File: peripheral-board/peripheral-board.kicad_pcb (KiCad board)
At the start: 2 copper layers, 165 x 100 mm, 152 parts, among them CON1001 AVR-ISP-10, IC1001 ATTINY48-A, P1001 Peripheral Bus, P1002 Power, P9001 VGA, P9002 VGA DSUB, SW2001 1, SW2002 2, SW2003 3, SW2004 4, SW2005 5, SW2006 6, SW2007 7, SW2008 8, SW2009 9, SW2010 0, SW2011 +, SW2012 ´, SW2013 BKSP, SW2014 TROLL, SW2015 §, SW2016 UP, SW2017 RMB, SW2018 Q, SW2019 W, SW2020 E, SW2021 R, SW2022 T, SW2023 Y, SW2024 U, SW2025 I, SW2026 O, SW2027 P, SW2028 Å, SW2029 ¨, SW2030 RETURN, SW2031 ALT_GR, SW2032 <, SW2033 LEFT, SW2034 MMB, SW2035 A, SW2036 S, SW2037 D, SW2038 F, SW2039 G, SW2040 H, SW2041 J, SW2042 K, SW2043 L, SW2044 Ö, SW2045 Ä, SW2046 ', SW2047 ESC, SW2048 TAB, SW2049 ALT, SW2050 DOWN, SW2051 LMB, SW2052 SHIFT_L, SW2053 Z, SW2054 X, SW2055 C, SW2056 V, SW2057 B, SW2058 N, SW2059 M, SW2060 ,, SW2061 ., SW2062 -, SW2063 SHIFT_R, SW2064 FN_R, SW2065 SPACE, SW2066 FN_L, SW2067 RIGHT, SW2068 CTRL, SW2069 SPACE, U2001 4017, U2002 4017, U2003 74HC00, U6001 TCA0372

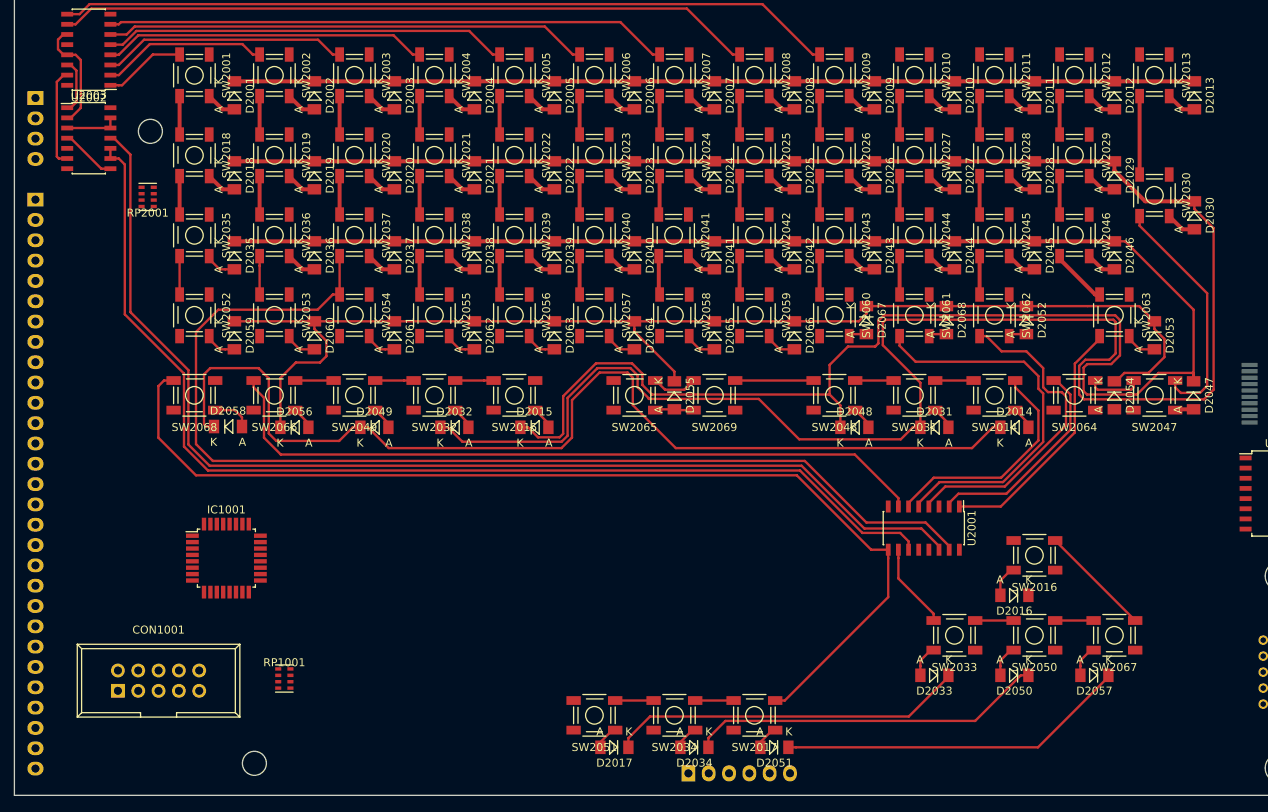
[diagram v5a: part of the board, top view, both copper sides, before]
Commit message: some more keyboard stuff fit on this side..
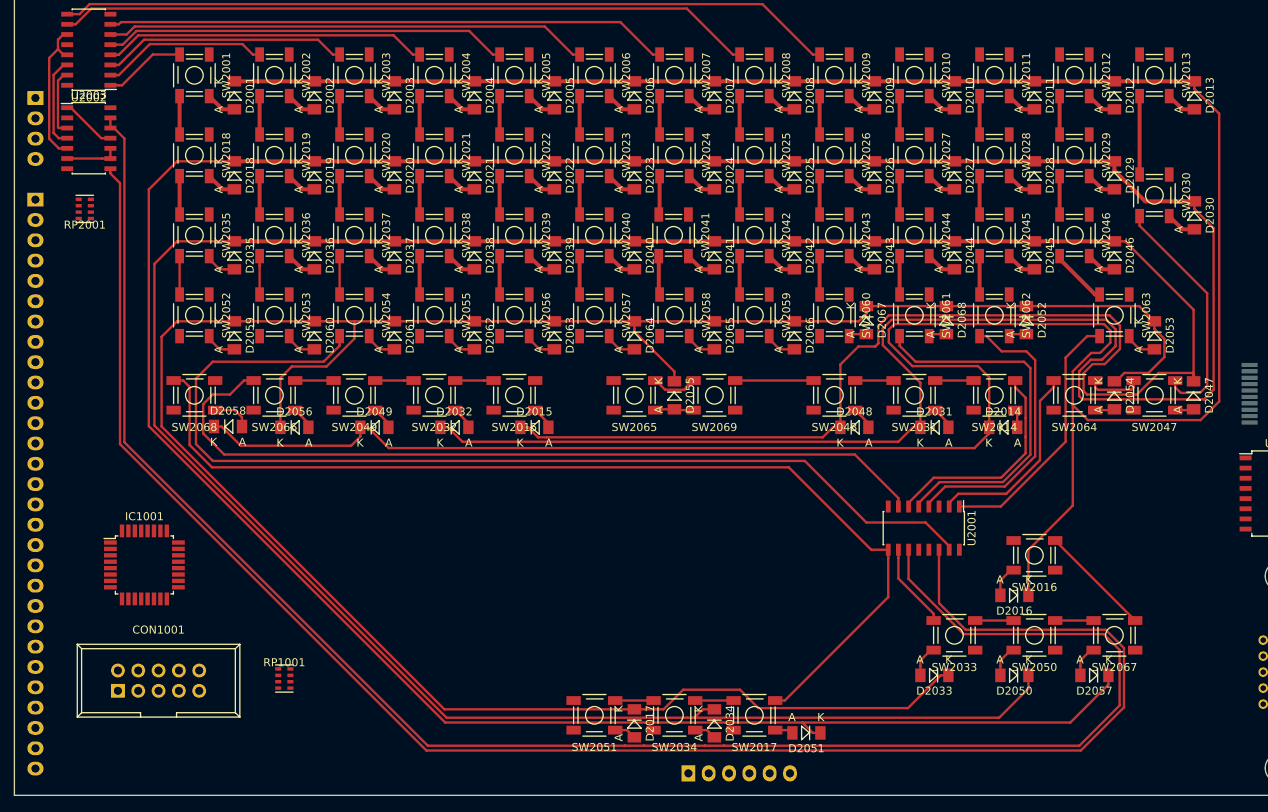
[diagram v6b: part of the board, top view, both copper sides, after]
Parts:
- removed REF** (x2): 3mm, Mounting_Holes:MountingHole_3mm
- moved IC1001 10.3 mm to (101.2, 121.2)
- moved RP2001 8.00 mm to (93.8, 76.7)
- moved D2051 4.39 mm to (184.0, 142.2)
- moved D2017 3.91 mm to (162.5, 141.0), turned to 270 degrees
- moved D2034 3.91 mm to (172.5, 141.0), turned to 270 degrees
- moved D2014 1.40 mm to (208.6, 104.0)
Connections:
- D2017 pad 1: /Keyboard/Q1 -> /Keyboard/Q3
- D2033 pad 1: /Keyboard/Q1 -> /Keyboard/Q3
- D2051 pad 1: /Keyboard/Q3 -> /Keyboard/Q1
- D2057 pad 1: /Keyboard/Q3 -> /Keyboard/Q1
- U2003 pad 1: /Keyboard/CLK -> Net-(U2003-Pad1)
- U2003 pad 10: Net-(U2001-Pad11) -> Net-(U2003-Pad10)
- U2003 pad 11: Net-(U2001-Pad14) -> Net-(U2003-Pad1)
- U2003 pad 12: Net-(U2003-Pad12) -> Net-(U2001-Pad11)
- U2003 pad 13: Net-(U2003-Pad12) -> Net-(U2001-Pad11)
- U2003 pad 2: Net-(U2002-Pad11) -> /Keyboard/~RESET
- U2003 pad 3: Net-(U2003-Pad12) -> Net-(U2002-Pad15)
- U2003 pad 4: Net-(U2003-Pad4) -> /Keyboard/CLK
- U2003 pad 5: /Keyboard/~RESET -> Net-(U2002-Pad11)
- U2003 pad 6: Net-(U2002-Pad15) -> Net-(U2003-Pad10)
- U2003 pad 8: Net-(U2003-Pad4) -> Net-(U2001-Pad14)
- U2003 pad 9: Net-(U2001-Pad11) -> Net-(U2003-Pad10)
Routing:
- net /Keyboard/Q1: track 339.0 -> 464.8 mm
- net /Keyboard/Q0: track 250.7 -> 372.0 mm
- net /Keyboard/Q2: track 302.9 -> 409.6 mm
- net /Keyboard/Q3: track 201.1 -> 297.0 mm
- net Net-(U2001-Pad11): track 138.2 -> 225.3 mm
- net Net-(U2001-Pad14): track 142.1 -> 219.0 mm
- net /Keyboard/COL14: track 105.6 -> 116.9 mm
- net Net-(U2003-Pad12): track 7.57 -> 0.00 mm
- net Net-(U2003-Pad4): track 7.43 -> 0.00 mm
- net Net-(U2003-Pad1): track 0.00 -> 7.43 mm
- net Net-(U2003-Pad10): track 0.00 -> 7.12 mm
- net /Keyboard/CLK: track 6.82 -> 12.3 mm
- net /Keyboard/COL2: track 178.9 -> 174.1 mm
- net Net-(U2002-Pad15): track 13.3 -> 8.95 mm
- net Net-(U2002-Pad11): track 14.7 -> 18.9 mm
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
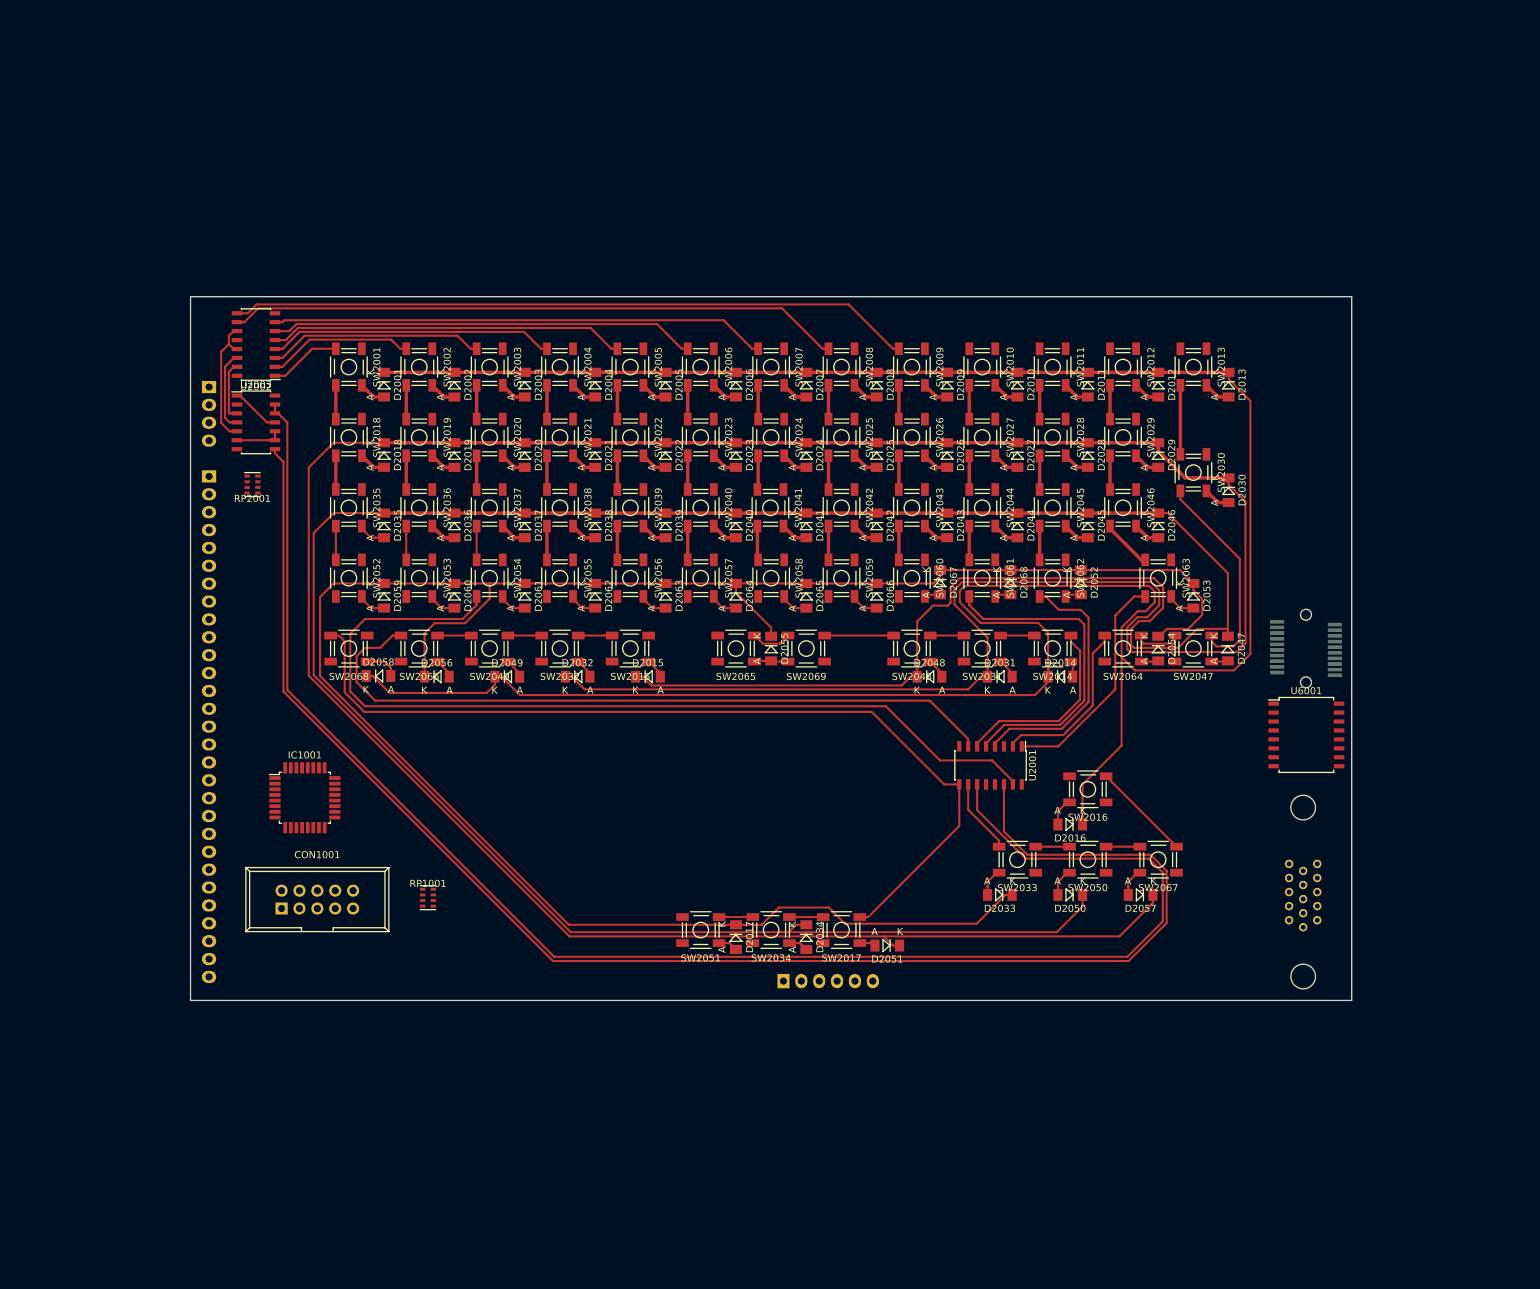
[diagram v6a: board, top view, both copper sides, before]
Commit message: added some audio circuitry
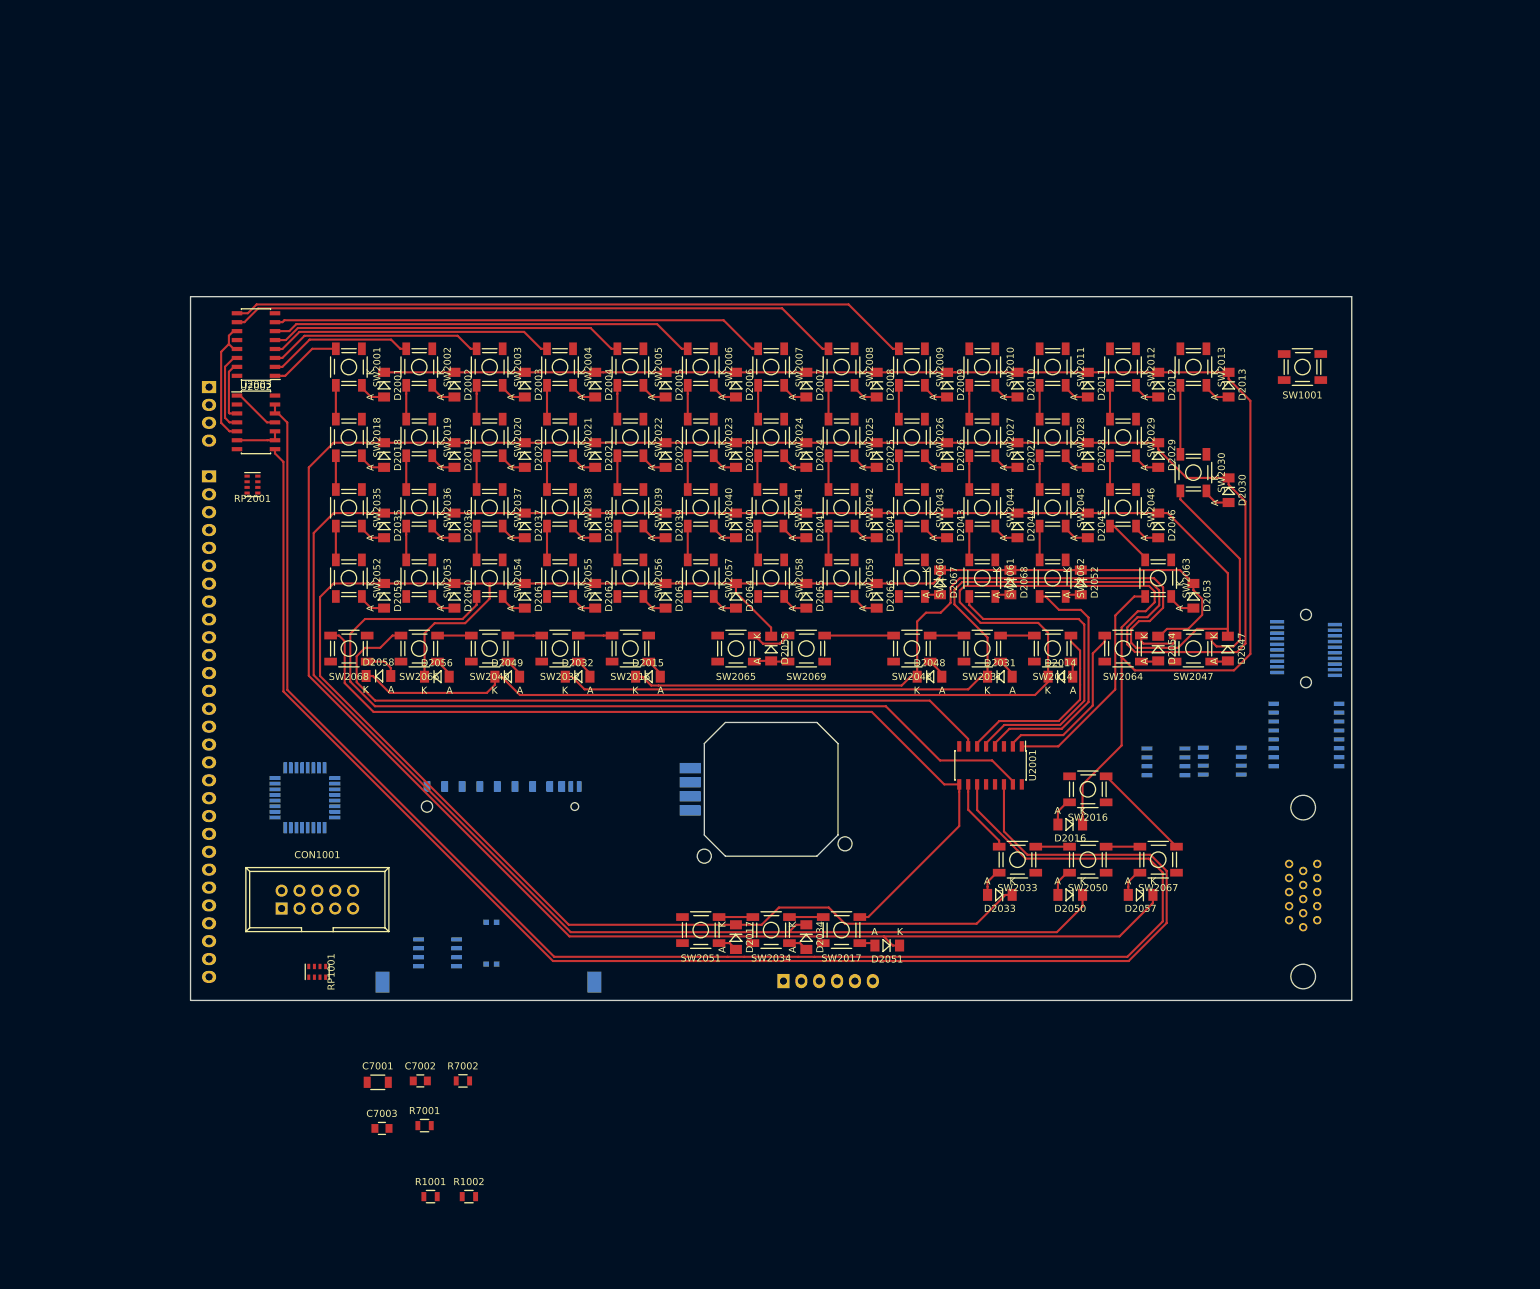
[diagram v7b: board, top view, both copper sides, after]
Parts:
- added C5001: C_Small, Capacitors_SMD:C_0603, B.Cu at (127.7, 138.9)
- added C5002: C_Small, Capacitors_SMD:C_0603, B.Cu at (127.7, 144.8)
- added C7001: 1u, Capacitors_SMD:C_1206, F.Cu at (111.6, 161.6)
- added C7002: C_Small, Capacitors_SMD:C_0805, F.Cu at (117.6, 161.4)
- added C7003: C_Small, Capacitors_SMD:C_0805, F.Cu at (112.2, 168.2)
- added CON7001: SD_Card, lib:TS-2198-01, B.Cu at (128.1, 120.4)
- added R1001: R, Resistors_SMD:R_0805, F.Cu at (119.1, 177.9)
- added R1002: R, Resistors_SMD:R_0805, F.Cu at (124.6, 177.9)
- added R7001: R, Resistors_SMD:R_0805, F.Cu at (118.3, 167.8)
- added R7002: R, Resistors_SMD:R_0805, F.Cu at (123.7, 161.4)
- added SW1001: Power, lib:SMD-TACT-5.2x5.2x2mm, F.Cu at (243.0, 60.0)
- added U3001: PSPNUB, lib:PSPNUB, B.Cu at (167.5, 120.0)
- added U5001: MCP7940N, Housings_SOIC:SOIC-8_3.9x4.9mm_Pitch1.27mm, B.Cu at (120.1, 143.2)
- added U6002: MCP4011, Housings_SOIC:SOIC-8_3.9x4.9mm_Pitch1.27mm, B.Cu at (223.6, 116.1)
- added U6003: MCP4011, Housings_SOIC:SOIC-8_3.9x4.9mm_Pitch1.27mm, B.Cu at (231.6, 116.0)
- IC1001, U6001: moved to B.Cu
- moved RP1001 18.9 mm to (103.0, 145.9), turned to 270 degrees
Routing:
- net /Keyboard/COL2: track 174.1 -> 173.2 mm
- net /Keyboard/COL16: track 137.3 -> 136.6 mm
- net /Keyboard/Q1: track 464.8 -> 464.3 mm
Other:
- outline, holes or cut-outs redrawn

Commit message: added audio jack
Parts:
- removed P9002: VGA DSUB, lib:HDDSUB-15-VGA
- added C4001: 1u, Capacitors_SMD:C_1206, B.Cu at (206.1, 23.4)
- added C4002: 1u, Capacitors_SMD:C_1206, B.Cu at (196.0, 14.9)
- added C4003: 10u, Capacitors_SMD:C_1206, B.Cu at (201.5, 14.9)
- added C4005: 680n, Capacitors_SMD:C_0805, B.Cu at (206.9, 16.8)
- added C4006: 2.2u, Capacitors_SMD:C_1206, B.Cu at (206.1, 30.1)
- added C4008: 120p, Capacitors_SMD:C_0805, B.Cu at (206.9, 10.5)
- added C4009: 10u, Capacitors_SMD:C_1206, B.Cu at (190.6, 15.8)
- added CON4001: BARREL_JACK, Connect:JACK_ALIM, B.Cu at (238.0, 55.0)
- added D4001: RBE2VA20ATR, Diodes_SMD:D_TUMD2, B.Cu at (178.0, 24.5)
- added D4002: RBE2VA20ATR, Diodes_SMD:D_TUMD2, B.Cu at (180.2, 30.6)
- added D4005: RBE2VA20ATR, Diodes_SMD:D_TUMD2, B.Cu at (191.0, 30.6)
- added D4006: 1n4148, Diodes_SMD:D_MiniMELF_Standard, B.Cu at (192.3, 24.4)
- added D4007: NSR0530HT1G, Diodes_SMD:D_SOD-323, B.Cu at (168.8, 30.6)
- added D4008: RBE2VA20ATR, Diodes_SMD:D_TUMD2, B.Cu at (169.0, 13.6)
- added J10001: DB15_FEMALE_HighDensity, lib:HDDSUB-15-VGA, B.Cu at (261.0, 28.0)
- added J6001: FCR1295, lib:FCR1295, B.Cu at (250.0, 99.7)
- added L4001: 8u2, Choke_SMD:Choke_SMD_1206_Standard, B.Cu at (185.0, 15.5)
- added L4002: 10u, Choke_SMD:Choke_SMD_1206_Standard, B.Cu at (198.3, 21.9)
- added L4003: 47u, Choke_SMD:Choke_SMD_7.3x7.3_H4.5, B.Cu at (167.8, 22.1)
- added U4001: AP1509, Housings_SOIC:SOIC-8_3.9x4.9mm_Pitch1.27mm, B.Cu at (178.1, 16.7)
- added U4002: LM27313, TO_SOT_Packages_SMD:SOT-23-5, B.Cu at (199.7, 29.5)
- added U4003: LT3652, Housings_SSOP:MSOP-12-1EP_3x4mm_Pitch0.65mm, B.Cu at (186.1, 23.3)
- added U5002: TL431, TO_SOT_Packages_SMD:SOT-23, B.Cu at (217.2, 29.9)
- added U5003: TL431, TO_SOT_Packages_SMD:SOT-23, B.Cu at (222.7, 29.9)
- moved U6001 46.1 mm to (224.0, 154.0)
- moved C5001 29.7 mm to (149.7, 158.9)
- moved C5002 29.7 mm to (149.7, 164.8)
- moved U5001 29.7 mm to (142.1, 163.2)
- moved SW1001 20.7 mm to (262.6, 66.6)
- moved CONN8001 16.1 mm to (242.0, 116.0)
